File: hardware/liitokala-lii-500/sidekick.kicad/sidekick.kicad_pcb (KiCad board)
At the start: 2 copper layers, 70 x 15 mm, 26 parts, among them J1 MCU, J2 USB, J3 LCD, J4 ST-Link V2, J5 EXPANSION, U1 STM32F103C8Tx, U2 XC6206PxxxMR, Y1 8 MHz

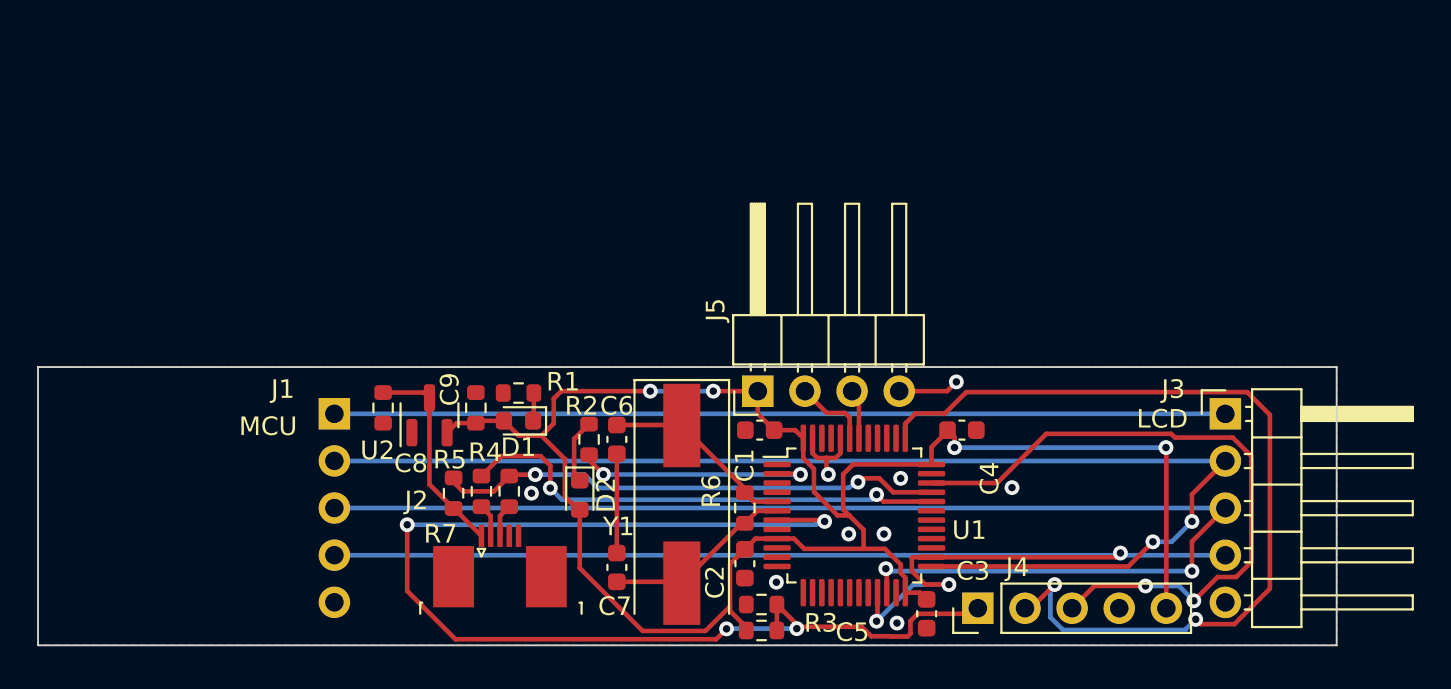
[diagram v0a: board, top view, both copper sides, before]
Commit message: liitokala-lii500: Update current project files to rev 2
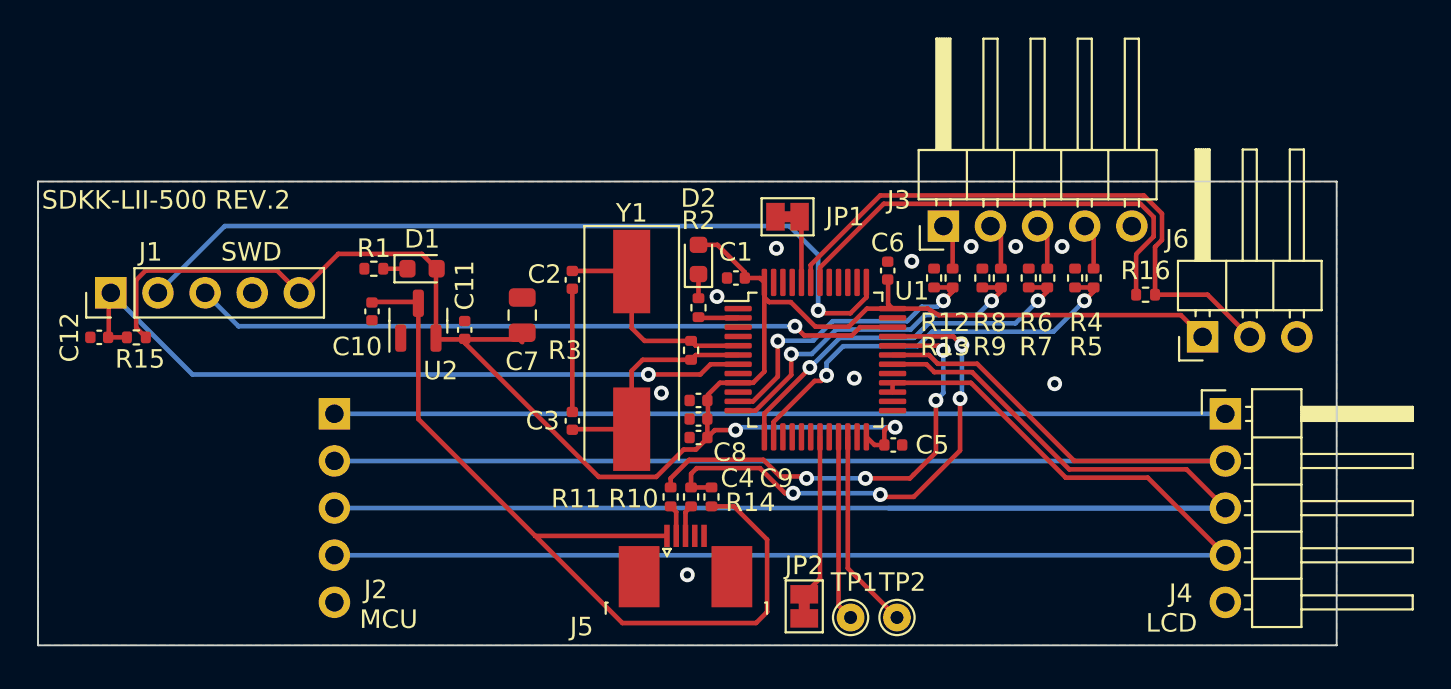
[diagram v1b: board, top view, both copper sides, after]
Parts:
- removed the C5 at (109.0, 83.8)
- removed the C6 at (101.2, 74.9)
- removed the J5 at (108.8, 72.3)
- added C11: 1uF, Capacitor_SMD:C_0402_1005Metric, F.Cu at (93.0, 69.0)
- added C12: 1uF, Capacitor_SMD:C_0402_1005Metric, F.Cu at (73.3, 69.4)
- added C2: 20pF, Capacitor_SMD:C_0402_1005Metric, F.Cu at (98.8, 66.3)
- added C3: 20pF, Capacitor_SMD:C_0402_1005Metric, F.Cu at (98.8, 73.9)
- added C8: 1uF, Capacitor_SMD:C_0402_1005Metric, F.Cu at (105.6, 72.8)
- added J3: VOLTAGES, Connector_PinHeader_2.54mm:PinHeader_1x05_P2.54mm_Horizontal, F.Cu at (118.8, 63.4)
- added J6: 1WIRE, Connector_PinHeader_2.54mm:PinHeader_1x03_P2.54mm_Horizontal, F.Cu at (132.8, 69.4)
- added JP1: Jumper_2_Bridged, Jumper:SolderJumper-2_P1.3mm_Bridged_Pad1.0x1.5mm, F.Cu at (110.4, 62.9)
- added JP2: Jumper_2_Bridged, Jumper:SolderJumper-2_P1.3mm_Bridged_Pad1.0x1.5mm, F.Cu at (111.3, 83.9)
- added R10: 22, Resistor_SMD:R_0402_1005Metric, F.Cu at (105.2, 78.0)
- added R11: 22, Resistor_SMD:R_0402_1005Metric, F.Cu at (104.1, 78.0)
- added R12: 47k, Resistor_SMD:R_0402_1005Metric, F.Cu at (119.3, 66.2)
- added R13: 47k, Resistor_SMD:R_0402_1005Metric, F.Cu at (118.3, 66.2)
- added R14: 4.7k, Resistor_SMD:R_0402_1005Metric, F.Cu at (106.3, 78.0)
- added R16: 150, Resistor_SMD:R_0402_1005Metric, F.Cu at (129.7, 67.1)
- added R6: 47k, Resistor_SMD:R_0402_1005Metric, F.Cu at (124.4, 66.2)
- added R8: 47k, Resistor_SMD:R_0402_1005Metric, F.Cu at (121.9, 66.2)
- added R9: 47k, Resistor_SMD:R_0402_1005Metric, F.Cu at (120.9, 66.2)
- added TP1: TestPoint, TestPoint:TestPoint_THTPad_D1.5mm_Drill0.7mm, F.Cu at (113.8, 84.5)
- added TP2: TestPoint, TestPoint:TestPoint_THTPad_D1.5mm_Drill0.7mm, F.Cu at (116.3, 84.5)
- C1: value 100n -> 100nF; footprint Capacitor_SMD:C_0603_1608Metric -> Capacitor_SMD:C_0402_1005Metric
- C10: renamed from C8; footprint Resistor_SMD:R_0603_1608Metric -> Capacitor_SMD:C_0402_1005Metric
- C4: renamed from C2; value 100n -> 100nF; footprint Capacitor_SMD:C_0603_1608Metric -> Capacitor_SMD:C_0402_1005Metric
- C5: renamed from C3; value 100n -> 100nF; footprint Capacitor_SMD:C_0603_1608Metric -> Capacitor_SMD:C_0402_1005Metric
- C6: renamed from C4; value 100n -> 100nF; footprint Capacitor_SMD:C_0603_1608Metric -> Capacitor_SMD:C_0402_1005Metric
- C7: value 20p -> 4.7uF; footprint Capacitor_SMD:C_0603_1608Metric -> Capacitor_SMD:C_0805_2012Metric
- C9: value 1uF -> 10nF; footprint Resistor_SMD:R_0603_1608Metric -> Capacitor_SMD:C_0402_1005Metric
- D2: value LED_PC13 -> LED_ACT
- J1: renamed from J4; value ST-Link V2 -> SWD
- R1, R2: footprint Resistor_SMD:R_0603_1608Metric -> Resistor_SMD:R_0402_1005Metric
- R15: renamed from R3; footprint Resistor_SMD:R_0603_1608Metric -> Resistor_SMD:R_0402_1005Metric
- R3: renamed from R6; footprint Resistor_SMD:R_0603_1608Metric -> Resistor_SMD:R_0402_1005Metric
- R4, R5: value 20R -> 47k; footprint Resistor_SMD:R_0603_1608Metric -> Resistor_SMD:R_0402_1005Metric
- R7: value 4.7k -> 47k; footprint Resistor_SMD:R_0603_1608Metric -> Resistor_SMD:R_0402_1005Metric
- U2: value XC6206PxxxMR -> XC6206
- moved J1 49.7 mm to (73.9, 67.0)
- moved R15 37.2 mm to (75.3, 69.4), turned to 180 degrees
- moved R5 34.0 mm to (125.9, 66.2)
- moved R4 33.5 mm to (126.9, 66.2), turned to -90 degrees
- moved R7 33.1 mm to (123.4, 66.2)
- moved C7 14.5 mm to (96.1, 68.2), turned to 90 degrees
- moved D2 14.2 mm to (105.6, 65.2), turned to 90 degrees
- moved C9 12.1 mm to (105.6, 74.8), turned to 180 degrees
- moved R1 10.3 mm to (88.1, 65.7)
- moved J5 10.0 mm to (104.9, 82.3)
- moved D1 9.71 mm to (90.7, 65.7), turned to 0 degrees
- moved C6 9.48 mm to (115.8, 65.8), turned to 90 degrees
- moved C5 9.28 mm to (116.1, 75.2), turned to 0 degrees
- moved R2 9.23 mm to (105.6, 67.8)
- moved R3 8.98 mm to (105.2, 70.1)
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- renumbered J1 to J2, J3 to J4, J2 to J5
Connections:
- net +5V renamed /5V
- net /PC13 renamed /LED_ACT
- C7 pad 1: Net-(C6-Pad1) -> +3V3
- C7 pad 2: /OSC_OUT -> GND
- J5 pad 2: Net-(J2-Pad2) -> Net-(J5-Pad2)
- J5 pad 3: Net-(J2-Pad3) -> Net-(J5-Pad3)
- R4 pad 1: Net-(J2-Pad3) -> Net-(J3-Pad4)
- R4 pad 2: /USBDP -> /ADC12_IN4
- R5 pad 1: Net-(J2-Pad2) -> /ADC12_IN4
- R5 pad 2: /USBDM -> GND
- R7 pad 1: VBUS -> /ADC12_IN3
- R7 pad 2: /USBDP -> GND
- U1 pad 11: unconnected-(U1-Pad11) -> /ADC12_IN1
- U1 pad 12: unconnected-(U1-Pad12) -> /ADC12_IN2
- U1 pad 13: unconnected-(U1-Pad13) -> /ADC12_IN3
- U1 pad 14: unconnected-(U1-Pad14) -> /ADC12_IN4
- U1 pad 19: GND -> /BOOT1
- U1 pad 21: //CS -> /USART3_TX
- U1 pad 22: /SCLK -> /USART3_RX
- U1 pad 25: /DATA -> unconnected-(U1-Pad25)
- U1 pad 26: //CS -> unconnected-(U1-Pad26)
- U1 pad 27: unconnected-(U1-Pad27) -> //CS
- U1 pad 28: unconnected-(U1-Pad28) -> //CS
- U1 pad 30: unconnected-(U1-Pad30) -> /SCLK
- U1 pad 31: unconnected-(U1-Pad31) -> /DATA
- U1 pad 42: /SCL_USART1_TX -> /USART1_TX
- U1 pad 43: /SDA_USART1_RX -> /USART1_RX
- U1 pad 44: GND -> /BOOT0
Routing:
- net VBUS: track 11.2 -> 47.2 mm
- net /USART1_RX: track 0.00 -> 32.4 mm
- net /NRST: track 66.4 -> 39.3 mm, vias 4 -> 1
- net /USART1_TX: track 0.00 -> 25.0 mm
- net /ADC12_IN4: track 0.00 -> 22.6 mm, vias 0 -> 2
- net /ADC12_IN3: track 0.00 -> 20.5 mm, vias 0 -> 2
- net /ADC12_IN2: track 0.00 -> 19.0 mm, vias 0 -> 2
- net /SCLK: track 70.0 -> 87.4 mm, vias 2 -> 0
- net /ADC12_IN1: track 0.00 -> 16.4 mm, vias 0 -> 2
- net /LED_ACT: track 13.3 -> 2.15 mm, vias 2 -> 0
- net /USART3_RX: track 0.00 -> 10.8 mm
- net /USART3_TX: track 0.00 -> 10.0 mm
- net /BOOT1: track 0.00 -> 8.84 mm
- net GND: track 7.61 -> 0.00 mm, vias 9 -> 10
- net Net-(C2-Pad1): track 0.00 -> 6.64 mm
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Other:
- board size 70 x 15 mm -> 70 x 25 mm
- board text added: "SDKK-LII-500 REV.2"

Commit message: liitokala-lii500: Updated kicad files to rev 3
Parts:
- added D3: SM4007PL, Diode_SMD:D_SOD-123, F.Cu at (89.3, 79.2)
- added D4: SM4007PL, Diode_SMD:D_SOD-123, F.Cu at (94.5, 77.7)
- added R17: 10K, Resistor_SMD:R_0402_1005Metric, F.Cu at (129.9, 71.8)
- added R18: 10K, Resistor_SMD:R_0402_1005Metric, F.Cu at (129.9, 72.9)
- J2: moved to F.Cu
- J4: moved to B.Cu
- J5: footprint Local:JUSHUO_AFC07-S05ECC-00_1x05_1MP_P0.5mm_Horizontal -> Local:JUSHUO_ AFA07-S05FCC-00_1x05_1MP_P1mm_Horizontal
- J6: value 1WIRE -> EXPAND; footprint Connector_PinHeader_2.54mm:PinHeader_1x03_P2.54mm_Horizontal -> Connector_PinHeader_2.54mm:PinHeader_1x04_P2.54mm_Horizontal
- Y1: footprint Crystal:Crystal_SMD_HC49-SD -> Crystal:Crystal_SMD_5032-2Pin_5.0x3.2mm
- moved J4 10.2 mm to (134.0, 83.7)
- moved J2 10.2 mm to (86.0, 83.7)
- moved R16 5.50 mm to (131.5, 72.3), turned to -90 degrees
- moved J6 2.52 mm to (130.3, 69.4)
- moved J3 2.48 mm to (116.3, 63.4)
- moved JP2 2.10 mm to (113.4, 83.9)
- moved TP1 2.10 mm to (115.9, 84.5)
- moved TP2 2.10 mm to (118.4, 84.5)
- moved R13 1.10 mm to (119.4, 66.2)
- moved R4 1.10 mm to (125.8, 66.2)
- moved R7 1.10 mm to (124.5, 66.2)
- moved R9 1.10 mm to (122.0, 66.2)
- moved R12 1.00 mm to (118.3, 66.2)
- moved R5 1.00 mm to (126.9, 66.2)
- moved R6 1.00 mm to (123.4, 66.2)
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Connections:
- C10 pad 1: VBUS -> +5V
- J5 pad 4: GND -> unconnected-(J5-Pad4)
- J6 pad 2: /USART1_RX -> /USART1_TX
- J6 pad 3: GND -> /USART1_RX
- U1 pad 27: //CS -> unconnected-(U1-Pad27)
- U1 pad 28: //CS -> /DATA
- U1 pad 29: unconnected-(U1-Pad29) -> /SCLK
- U1 pad 30: /SCLK -> //CS
- U1 pad 31: /DATA -> //CS
- U2 pad 3: VBUS -> +5V
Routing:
- net VBUS: track 47.2 -> 28.2 mm
- net /SCLK: track 87.4 -> 69.0 mm
- net +5V: track 0.00 -> 16.1 mm
- net /USART1_TX: track 25.0 -> 32.3 mm
- net /5V: track 48.0 -> 53.0 mm
- net /USART1_RX: track 32.4 -> 37.1 mm
- net +3V3: track 101.9 -> 104.0 mm
- net /OSC_OUT: track 12.5 -> 10.6 mm
- net /OSC_IN: track 12.4 -> 10.7 mm
- net //CS: track 70.3 -> 68.6 mm
- net /DATA: track 68.3 -> 69.8 mm
- net /ADC12_IN4: track 22.6 -> 23.6 mm
- net /ADC12_IN1: track 16.4 -> 17.4 mm
- net /ADC12_IN3: track 20.5 -> 21.6 mm
- net /ADC12_IN2: track 19.0 -> 20.0 mm
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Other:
- board text added: "PIN 1 (RED) ->"
- board text added: "PIN 1 <- (RED)"
- board text added: "SDKK-LII-500 REV.3"
- board text removed: "SDKK-LII-500 REV.2"

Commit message: liitokala-lii500: Add rev3 board files
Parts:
- added R19: 470R, Resistor_SMD:R_0402_1005Metric, F.Cu at (115.9, 81.0)
- added R20: 470R, Resistor_SMD:R_0402_1005Metric, F.Cu at (118.4, 81.0)
- added R21: 470R, Resistor_SMD:R_0402_1005Metric, F.Cu at (121.6, 72.7)
- added R22: 470R, Resistor_SMD:R_0402_1005Metric, F.Cu at (121.6, 71.7)
- added R23: 470R, Resistor_SMD:R_0402_1005Metric, F.Cu at (121.6, 70.7)
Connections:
- J2 pad 2: /DATA -> Net-(J2-Pad2)
- J2 pad 3: /SCLK -> Net-(J2-Pad3)
- J2 pad 4: //CS -> Net-(J2-Pad4)
- J4 pad 2: /DATA -> Net-(J2-Pad2)
- J4 pad 3: /SCLK -> Net-(J2-Pad3)
- J4 pad 4: //CS -> Net-(J2-Pad4)
- TP1 pad 1: /USART3_TX -> Net-(TP1-Pad1)
- TP2 pad 1: /USART3_RX -> Net-(TP2-Pad1)
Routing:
- net /DATA: track 69.8 -> 5.38 mm
- net /SCLK: track 69.0 -> 5.17 mm
- net Net-(J2-Pad2): track 0.00 -> 63.4 mm
- net //CS: track 68.6 -> 5.59 mm
- net Net-(J2-Pad3): track 0.00 -> 62.8 mm
- net Net-(J2-Pad4): track 0.00 -> 62.2 mm
- net /USART3_TX: track 10.9 -> 6.87 mm
- net Net-(TP2-Pad1): track 0.00 -> 2.99 mm
- net Net-(TP1-Pad1): track 0.00 -> 2.99 mm
- net /USART3_RX: track 11.7 -> 8.76 mm

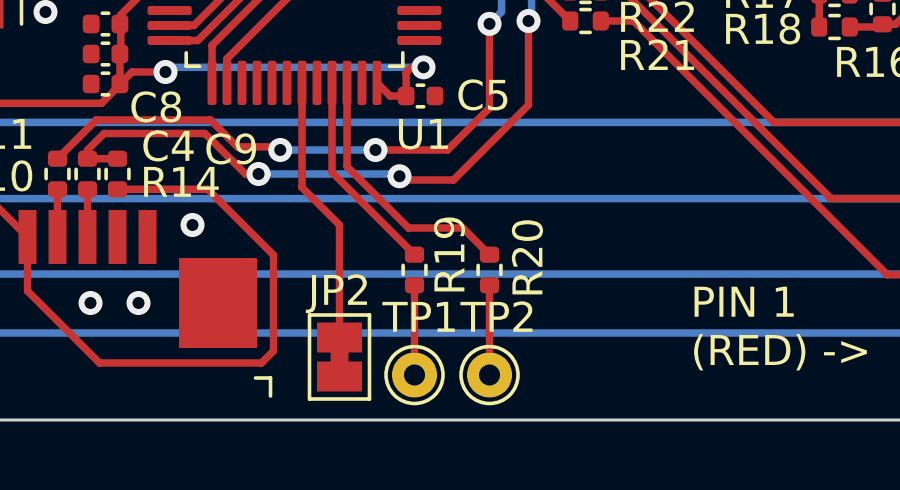
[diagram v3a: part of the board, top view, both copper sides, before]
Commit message: liitokala-lii500: Make debug UART pad labels more distinctive
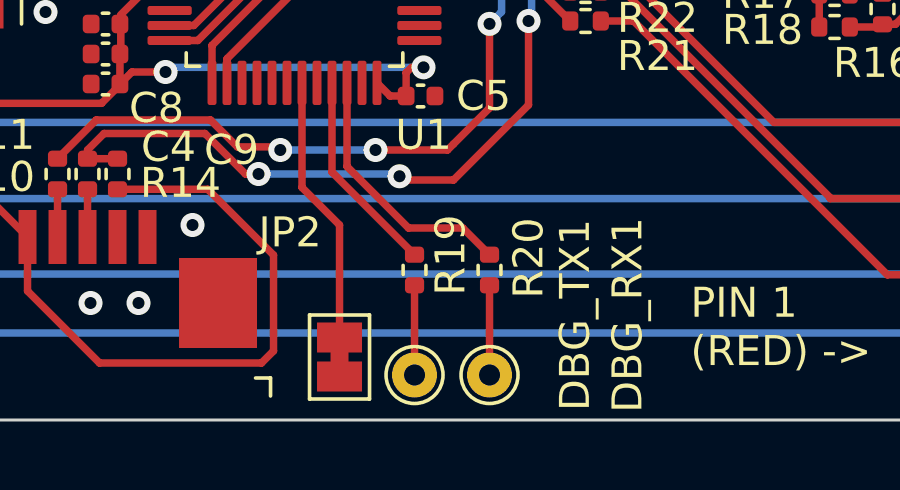
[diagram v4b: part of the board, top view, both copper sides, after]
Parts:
- renumbered TP2 to DBG_RX1, TP1 to DBG_TX1
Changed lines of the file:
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@@
-(kicad_pcb (version 20210722) (generator pcbnew)
+(kicad_pcb (version 20210824) (generator pcbnew)
   (general
     (thickness 1.6)
@@
   (net 56 "Net-(J2-Pad3)")
   (net 57 "Net-(J2-Pad4)")
-  (net 58 "Net-(TP1-Pad1)")
-  (net 59 "Net-(TP2-Pad1)")
+  (net 58 "Net-(R19-Pad1)")
+  (net 59 "Net-(R20-Pad1)")
   (footprint "Capacitor_SMD:C_0402_1005Metric" (layer "F.Cu")
     (at 98.5 73.9 -90)
@@
       (effects (font (size 1 1) (thickness 0.15)))
     )
-    (fp_poly (pts (xy -0.25 -0.3)
-      (xy 0.25 -0.3)
-      (xy 0.25 0.3)
-      (xy -0.25 0.3)) (layer "F.Cu") (width 0) (fill solid))
+    (fp_poly (pts
+        (xy -0.25 -0.3)
+        (xy 0.25 -0.3)
+        (xy 0.25 0.3)
+        (xy -0.25 0.3)
+      ) (layer "F.Cu") (width 0) (fill solid))
     (fp_line (start -1.4 -1) (end 1.4 -1) (layer "F.SilkS") (width 0.12))
     (fp_line (start 1.4 -1) (end 1.4 1) (layer "F.SilkS") (width 0.12))
@@
     (property "Sheetname" "")
     (attr exclude_from_pos_files)
-    (fp_text reference "TP1" (at 0.2 -1.9 180) (layer "F.SilkS")
+    (fp_text reference "DBG_TX1" (at 5.35 -2 270) (layer "F.SilkS")
       (effects (font (size 1 1) (thickness 0.15)))
     )
@@
     (fp_circle (center 0 0) (end 1.25 0) (layer "F.CrtYd") (width 0.05) (fill none))
     (pad "1" thru_hole circle locked (at 0 0) (size 1.5 1.5) (drill 0.7) (layers *.Cu *.Mask)
-      (net 58 "Net-(TP1-Pad1)") (pinfunction "1") (pintype "passive"))
+      (net 58 "Net-(R19-Pad1)") (pinfunction "1") (pintype "passive"))
   )
   (footprint "Resistor_SMD:R_0402_1005Metric" (layer "F.Cu")
@@
     (property "Sheetname" "")
     (attr exclude_from_pos_files)
-    (fp_text reference "JP2" (at 2.2 0 180) (layer "F.SilkS")
+    (fp_text reference "JP2" (at 4.15 -1.65 180) (layer "F.SilkS")
       (effects (font (size 1 1) (thickness 0.15)))
     )
@@
       (effects (font (size 1 1) (thickness 0.15)))
     )
-    (fp_poly (pts (xy -0.25 -0.3)
-      (xy 0.25 -0.3)
-      (xy 0.25 0.3)
-      (xy -0.25 0.3)) (layer "F.Cu") (width 0) (fill solid))
+    (fp_poly (pts
+        (xy -0.25 -0.3)
+        (xy 0.25 -0.3)
+        (xy 0.25 0.3)
+        (xy -0.25 0.3)
+      ) (layer "F.Cu") (width 0) (fill solid))
     (fp_line (start -1.4 -1) (end 1.4 -1) (layer "F.SilkS") (width 0.12))
     (fp_line (start -1.4 1) (end -1.4 -1) (layer "F.SilkS") (width 0.12))
@@
     (fp_line (start 0.525 -0.27) (end 0.525 0.27) (layer "F.Fab") (width 0.1))
     (pad "1" smd roundrect locked (at -0.51 0 90) (size 0.54 0.64) (layers "F.Cu" "F.Paste" "F.Mask") (roundrect_rratio 0.25)
-      (net 58 "Net-(TP1-Pad1)") (pintype "passive"))
+      (net 58 "Net-(R19-Pad1)") (pintype "passive"))
     (pad "2" smd roundrect locked (at 0.51 0 90) (size 0.54 0.64) (layers "F.Cu" "F.Paste" "F.Mask") (roundrect_rratio 0.25)
       (net 16 "/USART3_TX") (pintype "passive"))
@@
     (property "Sheetname" "")
     (attr exclude_from_pos_files)
-    (fp_text reference "TP2" (at 0.3 -1.9) (layer "F.SilkS")
+    (fp_text reference "DBG_RX1" (at 4.6 -2 90) (layer "F.SilkS")
       (effects (font (size 1 1) (thickness 0.15)))
     )
@@
     (fp_circle (center 0 0) (end 1.25 0) (layer "F.CrtYd") (width 0.05) (fill none))
     (pad "1" thru_hole circle locked (at 0 0) (size 1.5 1.5) (drill 0.7) (layers *.Cu *.Mask)
-      (net 59 "Net-(TP2-Pad1)") (pinfunction "1") (pintype "passive"))
+      (net 59 "Net-(R20-Pad1)") (pinfunction "1") (pintype "passive"))
   )
   (footprint "Resistor_SMD:R_0402_1005Metric" (layer "F.Cu")
@@
     (fp_line (start -0.525 0.27) (end -0.525 -0.27) (layer "F.Fab") (width 0.1))
     (pad "1" smd roundrect locked (at -0.51 0 90) (size 0.54 0.64) (layers "F.Cu" "F.Paste" "F.Mask") (roundrect_rratio 0.25)
-      (net 59 "Net-(TP2-Pad1)") (pintype "passive"))
+      (net 59 "Net-(R20-Pad1)") (pintype "passive"))
     (pad "2" smd roundrect locked (at 0.51 0 90) (size 0.54 0.64) (layers "F.Cu" "F.Paste" "F.Mask") (roundrect_rratio 0.25)
       (net 17 "/USART3_RX") (pintype "passive"))
